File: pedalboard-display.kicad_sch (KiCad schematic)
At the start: 14 parts, among them J1 Conn_01x03_Pin, J2 Conn_01x03_Pin, J3 OLED

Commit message: Add 3d models for JST connectors
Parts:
- J1, J2: footprint Connector_JST:JST_PH_B3B-PH-SM4-TB_1x03-1MP_P2.00mm_Vertical -> Library:JST_PH_B3B-PH-SM4-TB_1x03-1MP_P2.00mm_Vertical
- J3: footprint Connector_JST:JST_PH_B4B-PH-SM4-TB_1x04-1MP_P2.00mm_Vertical -> Library:JST_PH_B4B-PH-SM4-TB_1x04-1MP_P2.00mm_Vertical
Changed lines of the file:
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@@
 			)
 		)
-		(property "Footprint" "Connector_JST:JST_PH_B3B-PH-SM4-TB_1x03-1MP_P2.00mm_Vertical"
+		(property "Footprint" "Library:JST_PH_B3B-PH-SM4-TB_1x03-1MP_P2.00mm_Vertical"
 			(at 110.49 35.56 0)
 			(effects
@@
 			)
 		)
-		(property "Footprint" "Connector_JST:JST_PH_B3B-PH-SM4-TB_1x03-1MP_P2.00mm_Vertical"
+		(property "Footprint" "Library:JST_PH_B3B-PH-SM4-TB_1x03-1MP_P2.00mm_Vertical"
 			(at 64.77 130.81 0)
 			(effects
@@
 			)
 		)
-		(property "Footprint" "Connector_JST:JST_PH_B4B-PH-SM4-TB_1x04-1MP_P2.00mm_Vertical"
+		(property "Footprint" "Library:JST_PH_B4B-PH-SM4-TB_1x04-1MP_P2.00mm_Vertical"
 			(at 60.96 160.02 0)
 			(effects

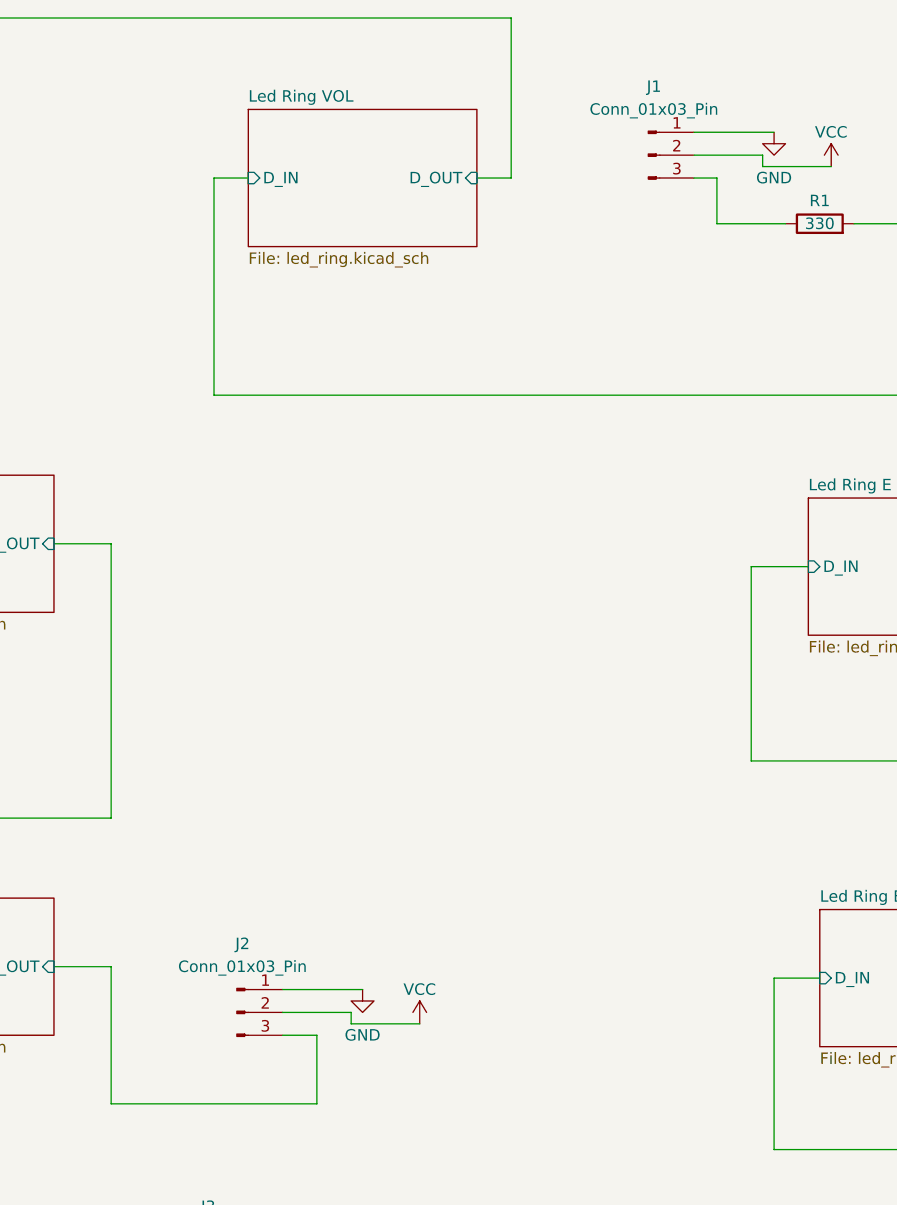
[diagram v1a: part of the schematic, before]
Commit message: Small text improvments
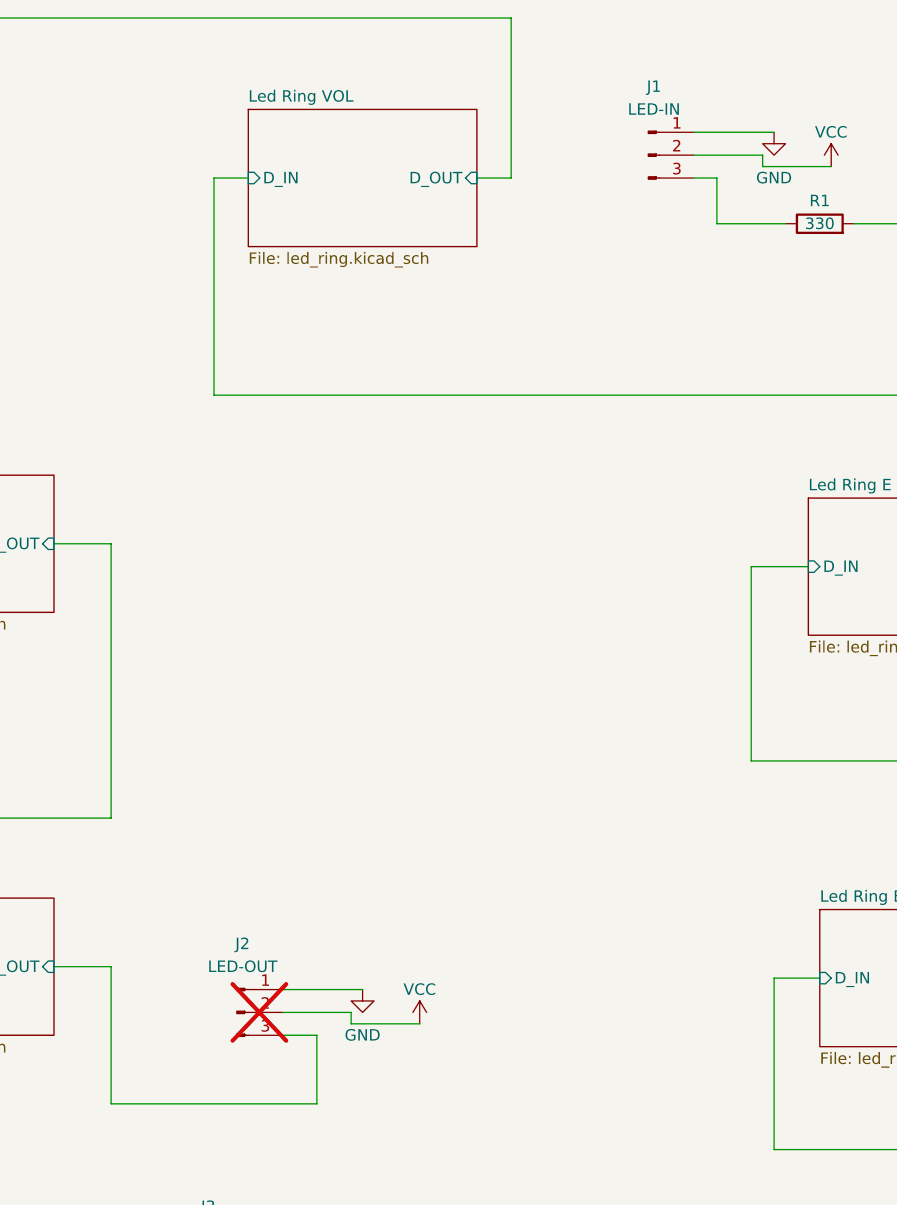
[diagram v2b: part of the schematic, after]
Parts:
- J1: value Conn_01x03_Pin -> LED-IN
- J2: value Conn_01x03_Pin -> LED-OUT; now not fitted
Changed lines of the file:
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@@
 			)
 		)
-		(property "Value" "Conn_01x03_Pin"
+		(property "Value" "LED-IN"
 			(at 111.125 30.48 0)
 			(effects
@@
 		(in_bom yes)
 		(on_board yes)
-		(dnp no)
+		(dnp yes)
 		(fields_autoplaced yes)
 		(property "Reference" "J2"
@@
 			)
 		)
-		(property "Value" "Conn_01x03_Pin"
+		(property "Value" "LED-OUT"
 			(at 65.405 125.73 0)
 			(effects

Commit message: Fix title
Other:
- title: Pedalboard Dispaly -> Pedalboard Display
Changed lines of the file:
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@@
 	(paper "A4")
 	(title_block
-		(title "Pedalboard Dispaly")
+		(title "Pedalboard Display")
 		(date "2024-10-05")
 		(rev "0.0.0-RC1")

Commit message: Add Mounting Holes
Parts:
- added H1, H2, H3, H4, H5: MountingHole, MountingHole:MountingHole_2.5mm, symbol Mechanical:MountingHole
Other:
- moved on the sheet: FID1, FID2, FID3, FID4

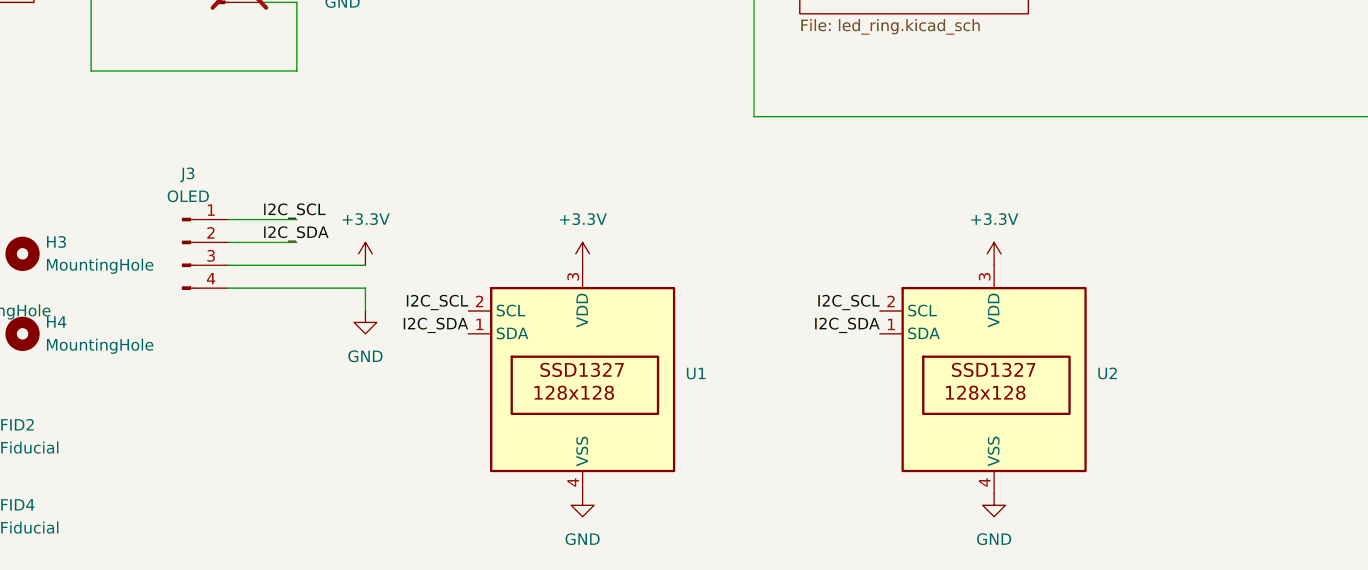
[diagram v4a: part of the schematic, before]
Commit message: Add optional pull up resistors
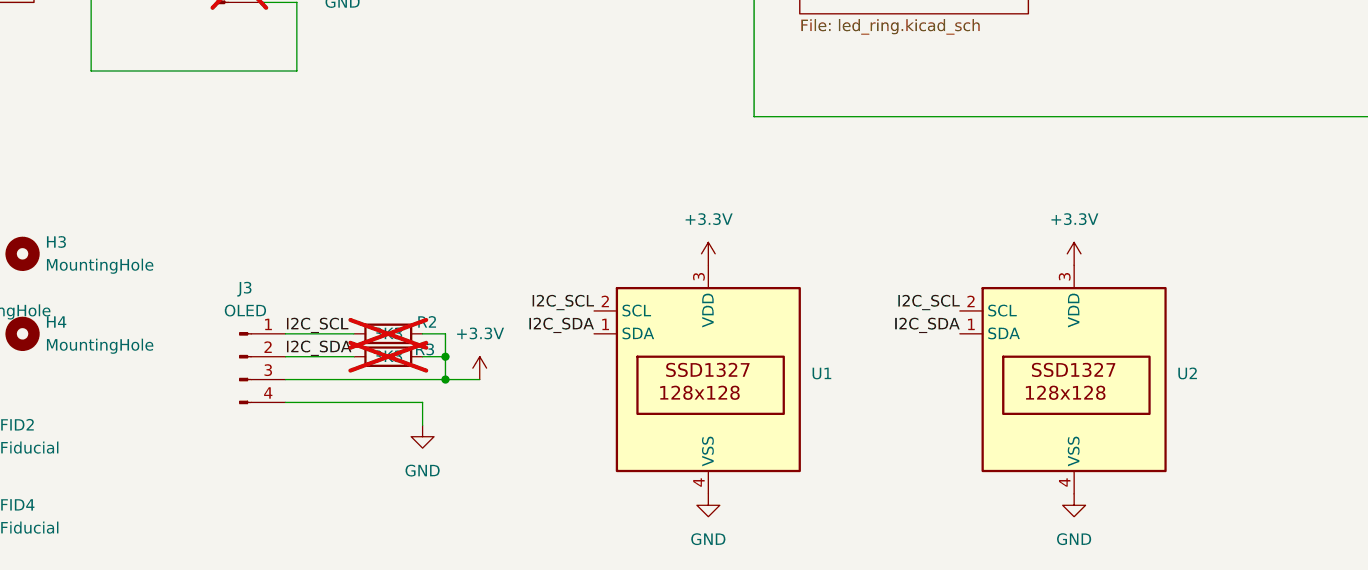
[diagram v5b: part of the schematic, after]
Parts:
- added R2, R3: 3K3, Resistor_SMD:R_0805_2012Metric, symbol Device:R
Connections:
- net +3.3V: now also R2.1, R3.1
- net I2C_SCL: now also R2.2
- net I2C_SDA: now also R3.2
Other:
- moved on the sheet: J3, U1, U2
